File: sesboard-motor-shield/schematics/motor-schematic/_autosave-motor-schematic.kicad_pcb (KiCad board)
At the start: 2 copper layers, 32 parts, among them J1 Barrel_Jack, J10 MOTOR_D_OUT, J2 EXTERNAL_MOTOR_POWER, J3 MOTOR_C_OUT, J3 SESBOARD_1, J4 MOTOR_D_OUT, J4 SESBOARD_2, J5 MOTOR_A_OUT, J5 SERVO1, J6 MOTOR_B_OUT, J6 SERVO2, J7 MOTOR_A_OUT, J7 SERVO1, J8 MOTOR_B_OUT, J8 SERVO2, J9 MOTOR_C_OUT, Q1 Q_NMOS_DGS, Q2 TIP3055, U1 LM317_SOT-223, U2 L293D, U3 L293D, U4 AMS1117-5.0, U5 L293D

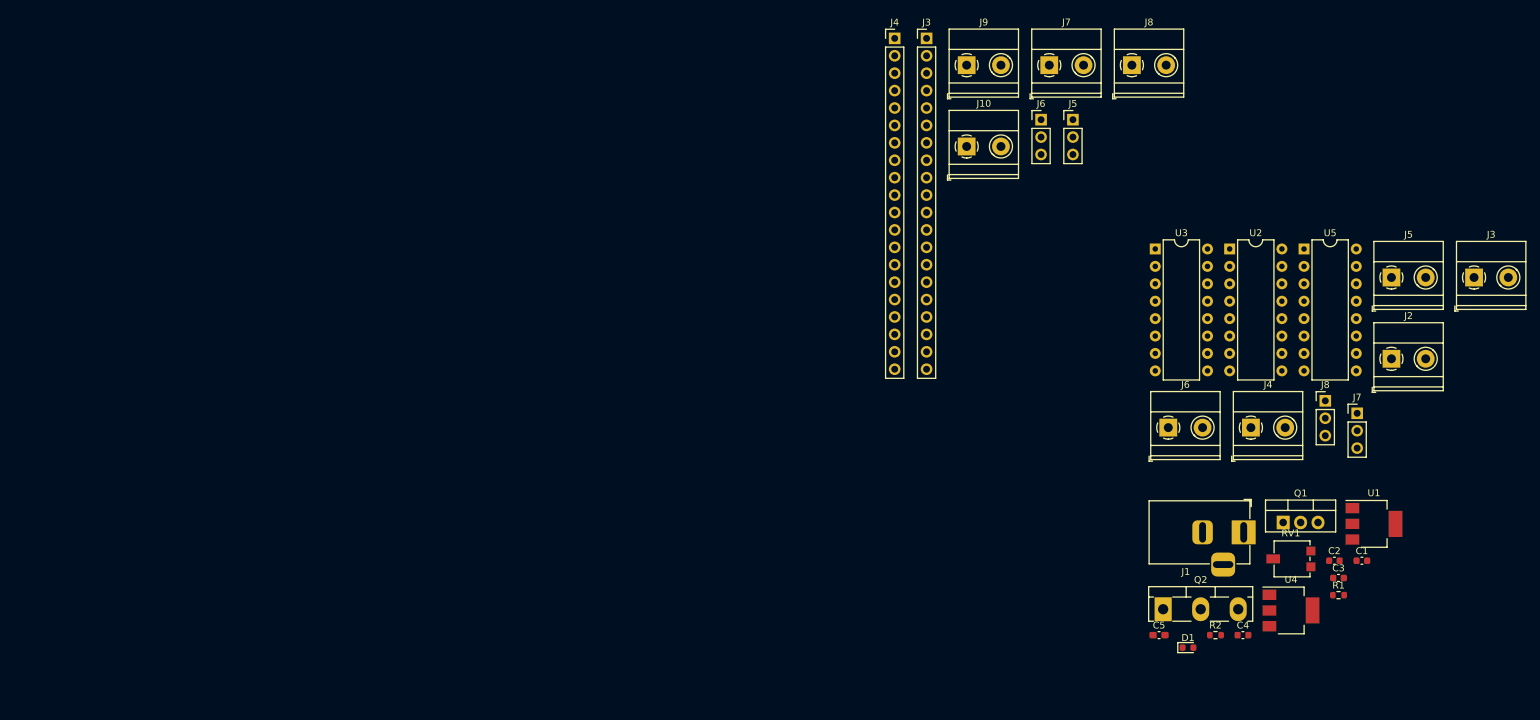
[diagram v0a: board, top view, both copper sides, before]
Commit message: added power toggle
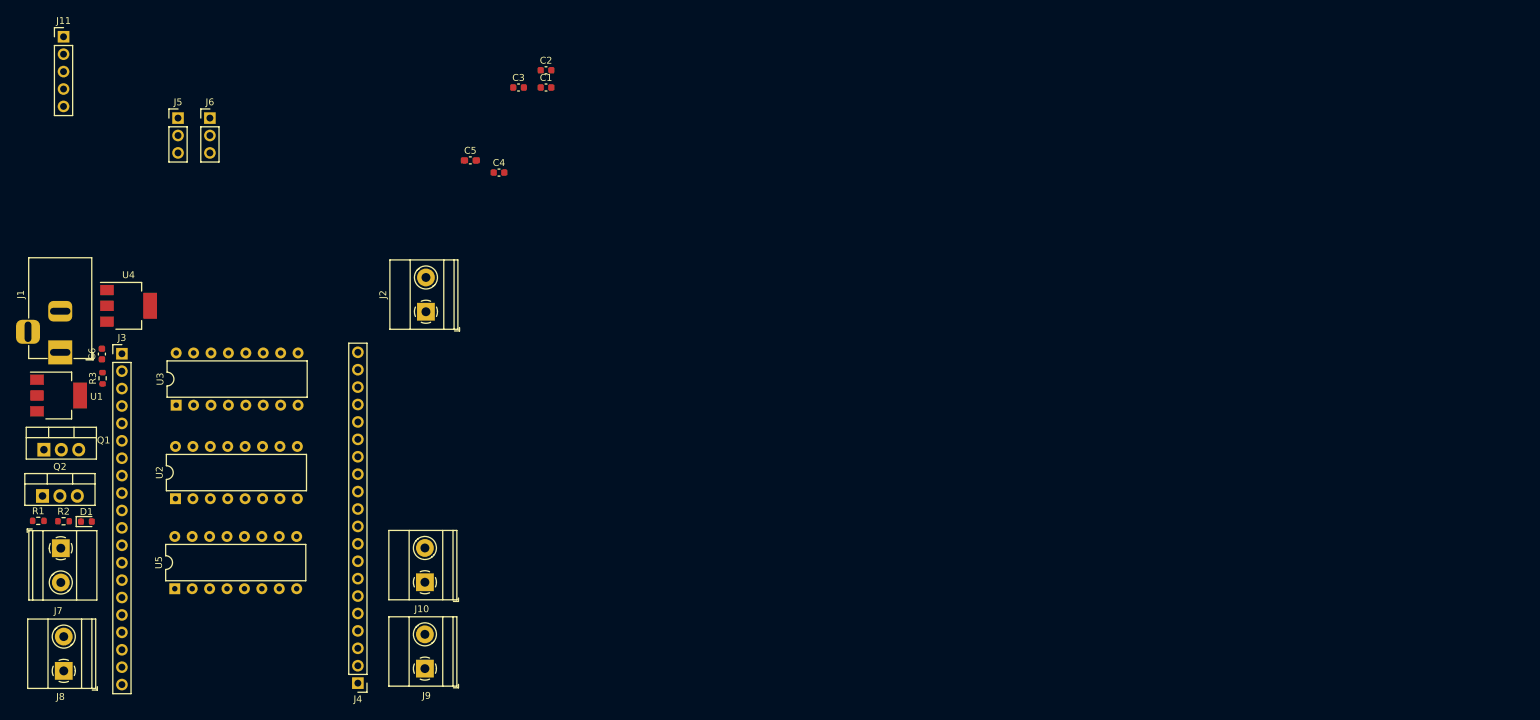
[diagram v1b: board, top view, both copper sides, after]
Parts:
- removed the J3 at (275.4, 61.5)
- removed the J3 at (195.6, 26.7)
- removed the J4 at (190.9, 26.7)
- removed the J4 at (242.9, 83.5)
- removed the J5 at (216.9, 38.5)
- removed the J5 at (263.4, 61.5)
- removed the J6 at (212.3, 38.5)
- removed the J6 at (230.8, 83.5)
- removed the J7 at (213.5, 30.6)
- removed the J7 at (258.4, 81.4)
- removed the J8 at (253.7, 79.5)
- removed the J8 at (225.5, 30.6)
- removed RV1: R_Potentiometer_Trim_US, Potentiometer_SMD:Potentiometer_Vishay_TS53YL_Vertical
- added C6: 0.1uF, Capacitor_SMD:C_0603_1608Metric, F.Cu at (75.3, 72.7)
- added J11: STEPPER_TERMINAL, Connector_PinHeader_2.54mm:PinHeader_1x05_P2.54mm_Vertical, F.Cu at (69.7, 26.4)
- added J3: Conn_01x20_Female, Connector_PinHeader_2.54mm:PinHeader_1x20_P2.54mm_Vertical, F.Cu at (78.2, 72.7)
- added J4: Conn_01x20_Female, Connector_PinHeader_2.54mm:PinHeader_1x20_P2.54mm_Vertical, F.Cu at (112.6, 120.7)
- added J5: SERVO1, Connector_PinHeader_2.54mm:PinHeader_1x03_P2.54mm_Vertical, F.Cu at (86.4, 38.3)
- added J6: SERVO2, Connector_PinHeader_2.54mm:PinHeader_1x03_P2.54mm_Vertical, F.Cu at (91.0, 38.3)
- added J7: MOTOR_A_OUT, TerminalBlock_Phoenix:TerminalBlock_Phoenix_MKDS-1,5-2_1x02_P5.00mm_Horizontal, F.Cu at (69.3, 101.0)
- added J8: MOTOR_B_OUT, TerminalBlock_Phoenix:TerminalBlock_Phoenix_MKDS-1,5-2_1x02_P5.00mm_Horizontal, F.Cu at (69.7, 118.9)
- added R3: 2K, Resistor_SMD:R_0603_1608Metric, F.Cu at (75.4, 76.3)
- C1: value C -> 1uF
- Q2: footprint Package_TO_SOT_THT:TO-218-3_Vertical -> Package_TO_SOT_THT:TO-220-3_Vertical
- R1: value 510R -> 240R
- moved U1 192.8 mm to (69.0, 78.8)
- moved R1 190.0 mm to (66.0, 97.1)
- moved Q1 181.1 mm to (66.8, 86.7)
- moved U4 175.3 mm to (79.2, 65.7)
- moved J1 174.6 mm to (69.2, 72.5), turned to -90 degrees
- moved U5 172.0 mm to (85.9, 106.9), turned to 90 degrees
- moved R2 168.8 mm to (69.7, 97.1)
- moved Q2 164.3 mm to (66.6, 93.4)
- moved D1 161.7 mm to (73.0, 97.2)
- moved U2 158.0 mm to (86.0, 93.8), turned to 90 degrees
- moved U3 144.6 mm to (86.1, 80.2), turned to 90 degrees
- moved J2 141.0 mm to (122.6, 66.5), turned to 90 degrees
- moved C3 139.4 mm to (136.1, 33.8)
- moved C1 137.6 mm to (140.1, 33.8)
- moved C2 135.4 mm to (140.1, 31.3)
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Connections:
- net /dc_driver_ics/MOTOR_EXT+ renamed MOTOR_EXT+
- net /external_power/12V renamed 12V
- net /external_power/SERVO_5V renamed SERVO_5V
- J10 pad 1: /connectors/MOTOR_D_OUT+ -> MOTOR_D_OUT+
- J10 pad 2: /connectors/MOTOR_D_OUT- -> MOTOR_D_OUT-
- J9 pad 1: /connectors/MOTOR_C_OUT+ -> MOTOR_C_OUT-
- J9 pad 2: /connectors/MOTOR_C_OUT- -> MOTOR_C_OUT+
- R1 pad 2: GND -> Net-(R1-Pad2)
- U1 pad 1: GND -> Net-(R1-Pad2)
- U2 pad 1: /dc_driver_ics/ENC -> ENC
- U2 pad 10: /dc_driver_ics/IN7 -> IN7
- U2 pad 11: /dc_driver_ics/MOTOR_D_OUT- -> MOTOR_D_OUT-
- U2 pad 14: /dc_driver_ics/MOTOR_D_OUT+ -> MOTOR_D_OUT+
- U2 pad 15: /dc_driver_ics/IN8 -> IN8
- U2 pad 2: /dc_driver_ics/IN5 -> IN5
- U2 pad 3: /dc_driver_ics/MOTOR_C_OUT+ -> MOTOR_C_OUT+
- U2 pad 6: /dc_driver_ics/MOTOR_C_OUT- -> MOTOR_C_OUT-
- U2 pad 7: /dc_driver_ics/IN6 -> IN6
- U2 pad 9: /dc_driver_ics/END -> END
- U3 pad 1: /dc_driver_ics/ENA -> ENA
- U3 pad 10: /dc_driver_ics/IN3 -> IN3
- U3 pad 11: /dc_driver_ics/MOTOR_B_OUT+ -> MOTOR_B_OUT-
- U3 pad 14: /dc_driver_ics/MOTOR_B_OUT- -> MOTOR_B_OUT+
- U3 pad 15: /dc_driver_ics/IN4 -> IN4
- U3 pad 2: /dc_driver_ics/IN1 -> IN1
- U3 pad 3: /dc_driver_ics/MOTOR_A_OUT+ -> MOTOR_A_OUT+
- U3 pad 6: /dc_driver_ics/MOTOR_A_OUT- -> MOTOR_A_OUT-
- U3 pad 7: /dc_driver_ics/IN2 -> IN2
- U3 pad 9: /dc_driver_ics/ENB -> ENB
- U5 pad 10: /dc_driver_ics/STEPPER_IN3 -> STEPPER_IN3
- U5 pad 11: /dc_driver_ics/OUT3 -> OUT3
- U5 pad 14: /dc_driver_ics/OUT4 -> OUT4
- U5 pad 15: /dc_driver_ics/STEPPER_IN4 -> STEPPER_IN4
- U5 pad 2: /dc_driver_ics/STEPPER_IN1 -> STEPPER_IN1
- U5 pad 3: /dc_driver_ics/OUT1 -> OUT1
- U5 pad 6: /dc_driver_ics/OUT2 -> OUT2
- U5 pad 7: /dc_driver_ics/STEPPER_IN2 -> STEPPER_IN2
